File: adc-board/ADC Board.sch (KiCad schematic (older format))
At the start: 62 parts, among them J2 ST-LINK/V2, J3 USART3, J4 USART1, J5 UE27AC5410H, J7 AltPowerInput, J8 USBPowerJumper, J9 USART2, U0 STM32H743ZITx, U10 MCP1501-20E/SN, U13 3.3V Reg, U9 USBLC6-2SC6, Y1 NX3225GD-8.000M-EXS00A-CG04874

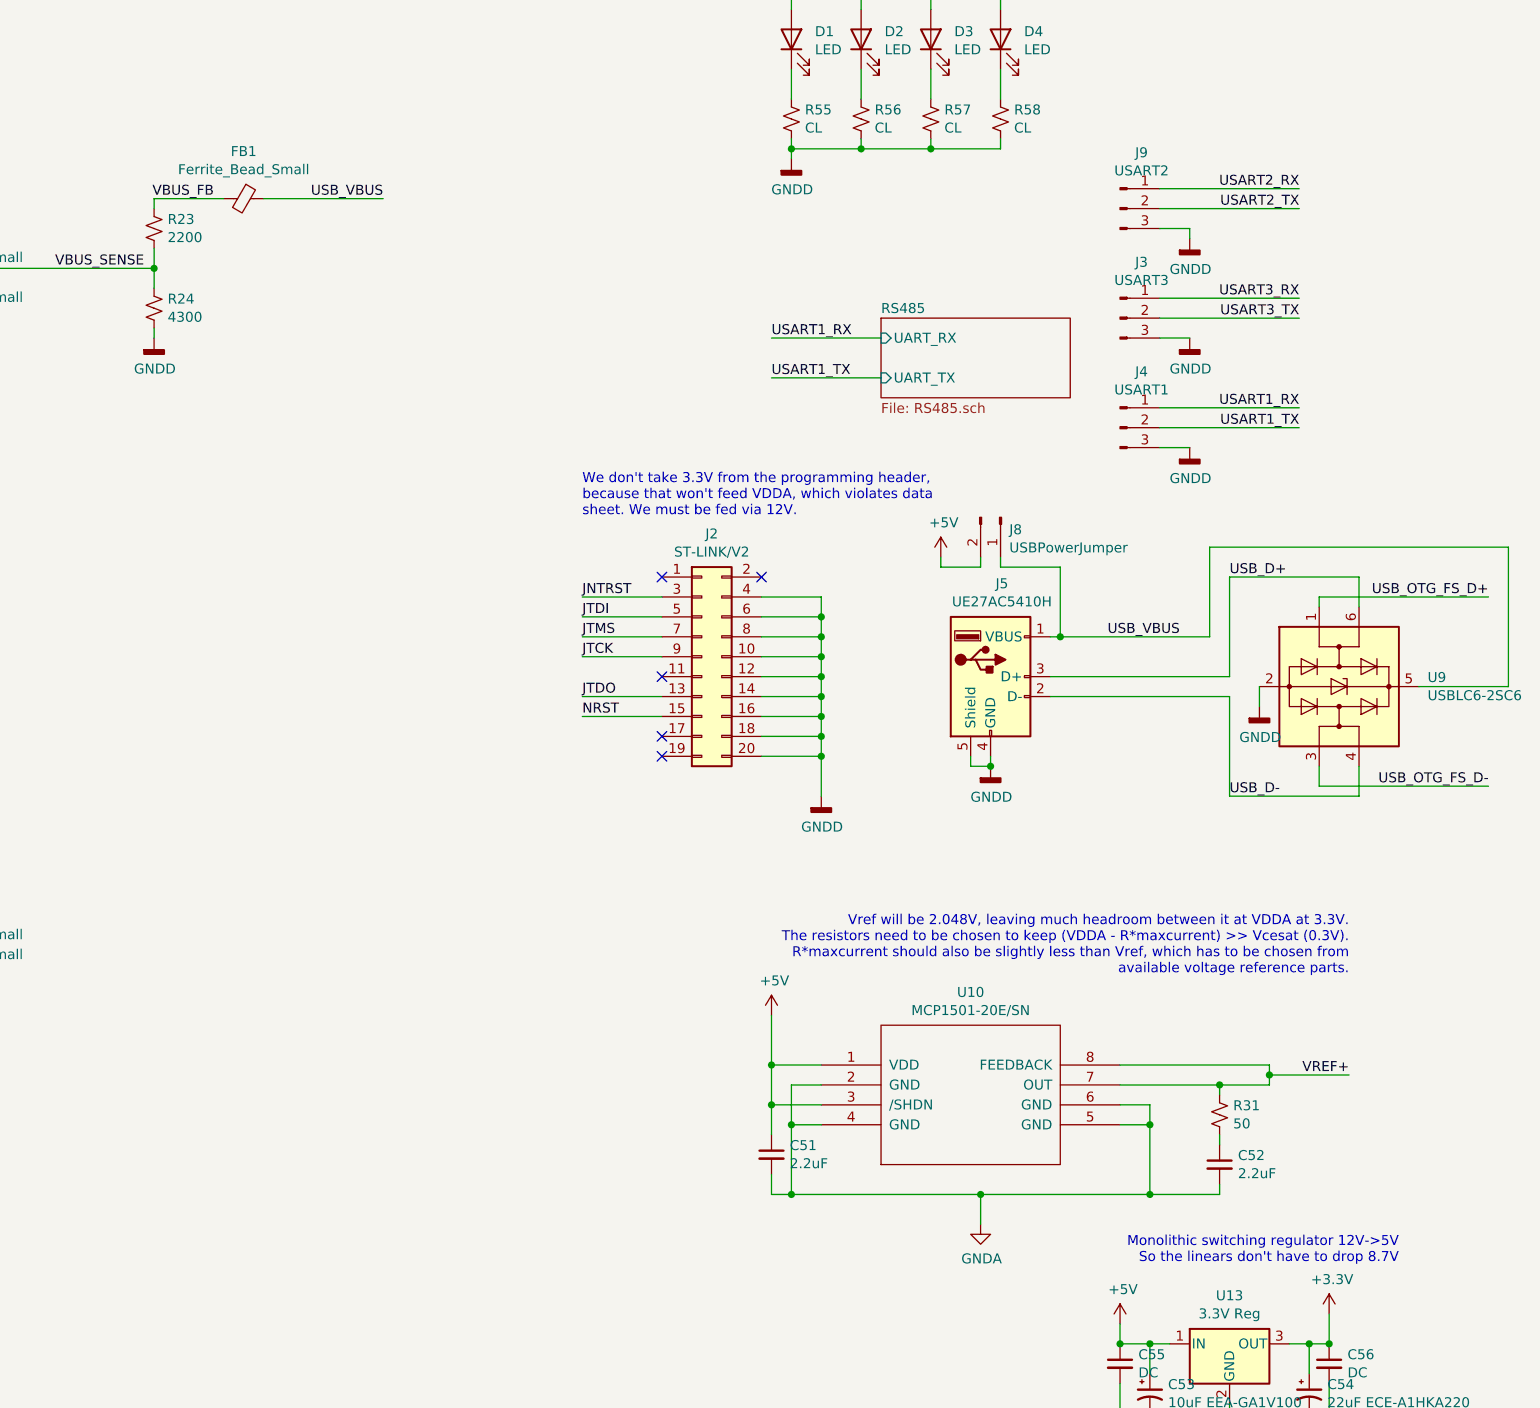
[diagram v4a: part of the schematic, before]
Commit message: move USB ferrite closer to connector; add VCC pad near BOOT pulldown
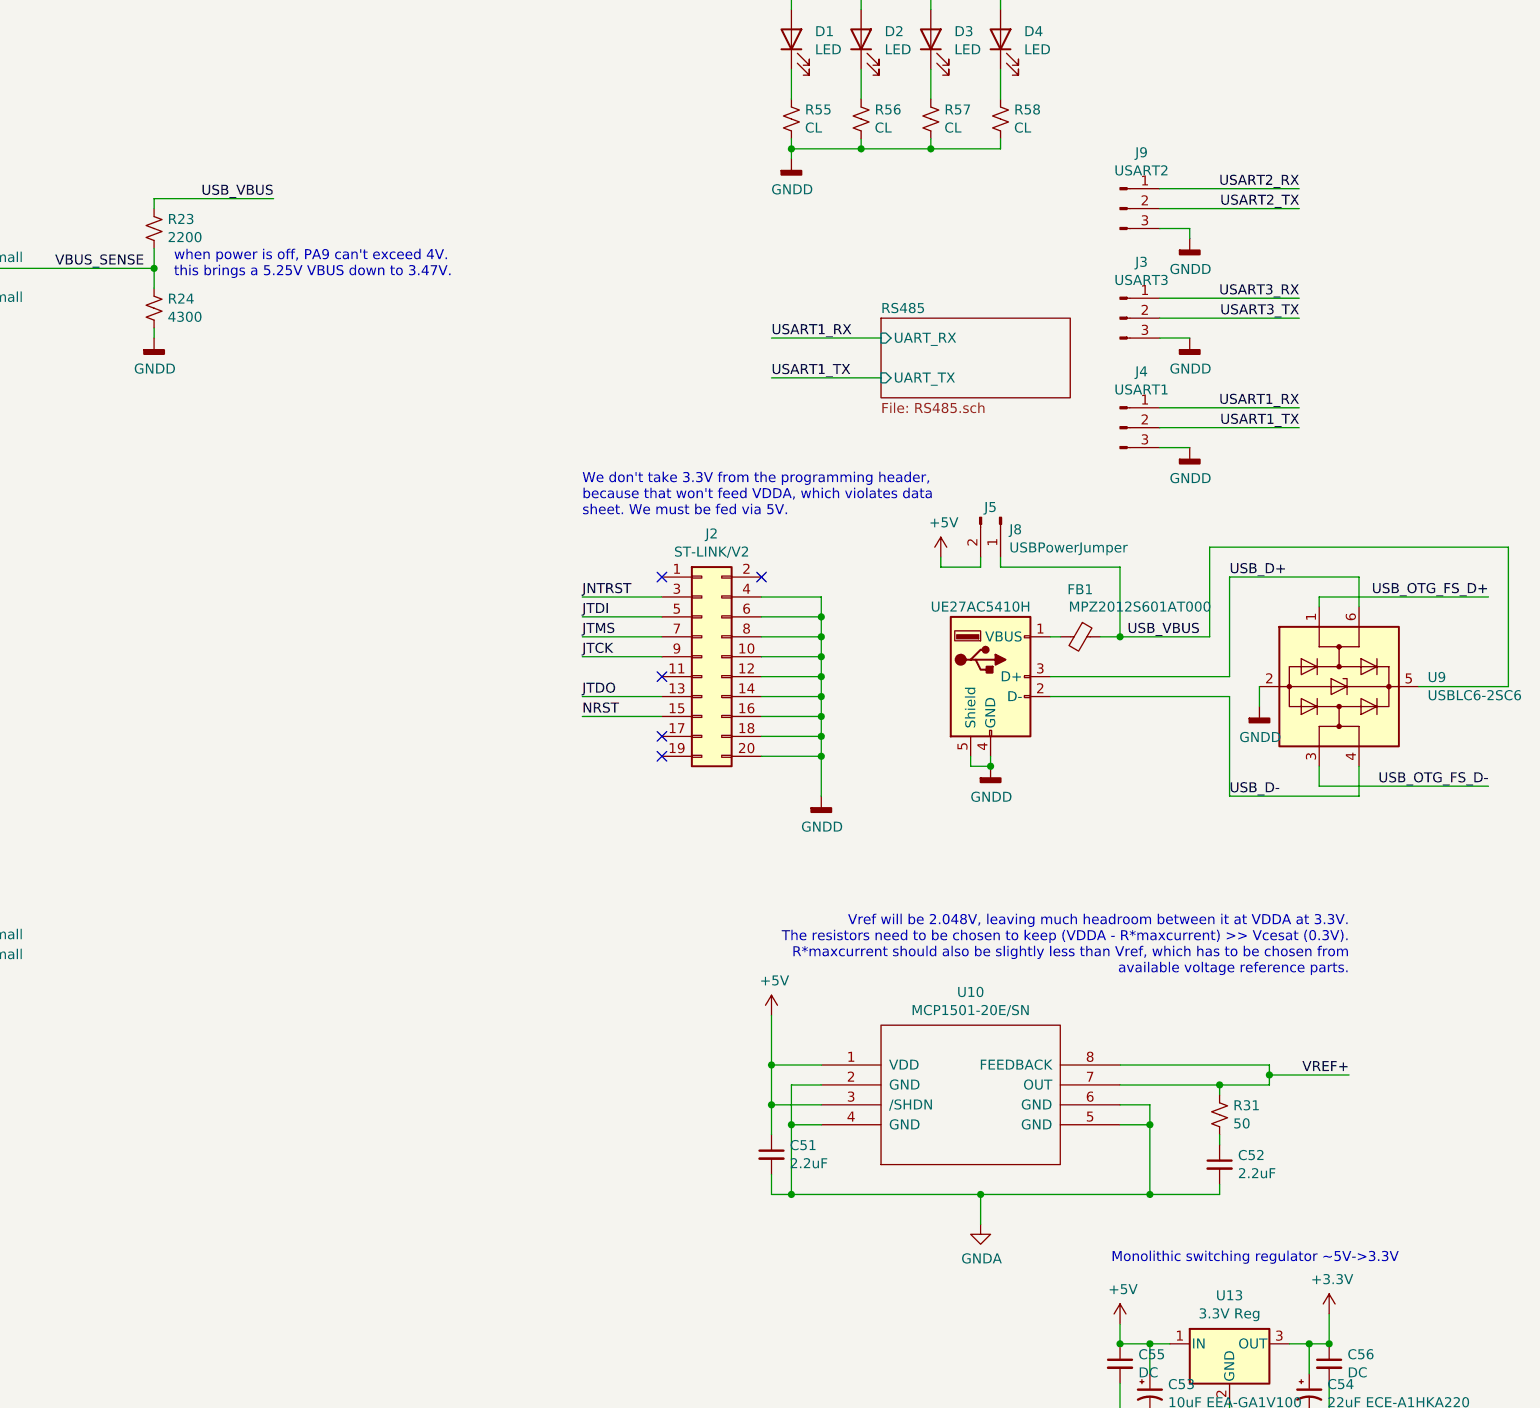
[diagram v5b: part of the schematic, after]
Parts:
- FB1: value Ferrite_Bead_Small -> MPZ2012S601AT000
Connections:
- net USB_VBUS: now also R23.1; no longer J5.1 (VBUS)
- net VBUS_FB: no longer names the net of FB1.2
- net VBUS_FB: now also J5.1 (VBUS); no longer R23.1
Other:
- note added: "Monolithic switching regulator ~~5V->3.3V"
- note added: "We don't take 3.3V from the programming header,\nbecause that won't feed VDDA, which violates data\nsheet. We must be fed via 5V."
- note added: "when power is off, PA9 can't exceed 4V.\nthis brings a 5.25V VBUS down to 3.47V."
- note removed: "Monolithic switching regulator 12V->5V\nSo the linears don't have to drop 8.7V"
- note removed: "We don't take 3.3V from the programming header,\nbecause that won't feed VDDA, which violates data\nsheet. We must be fed via 12V."
- moved on the sheet: FB1
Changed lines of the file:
@@
 U 1 1 62BFF5D3
 P 12500 5300
-F 0 "J5" H 12557 5767 50  0000 C CNN
-F 1 "UE27AC5410H" H 12557 5676 50  0000 C CNN
+F 0 "J5" H 12500 6150 50  0000 C CNN
+F 1 "UE27AC5410H" H 12450 5650 50  0000 C CNN
 F 2 "usbconnectors:USB_A_Molex_67643_Horizontal" H 12650 5250 50  0001 C CNN
 F 3 " ~" H 12650 5250 50  0001 C CNN
@@
 Reference STMicroelectronics Application Note AN4938\nfor details on basic STMH74x circuits
 Text Notes 14550 8250 2    50   ~ 0
-Monolithic switching regulator 12V->5V\nSo the linears don't have to drop 8.7V
+Monolithic switching regulator ~~5V->3.3V
 Text Notes 13850 9700 0    50   ~ 0
 Represents single connection between GNDD and GNDA\nnear the 5V regulator. Could be cut and choke inserted.
@@
 Don't intend to need this crystal circuit
 Text Notes 10450 4500 0    50   ~ 0
-We don't take 3.3V from the programming header,\nbecause that won't feed VDDA, which violates data\nsheet. We must be fed via 12V.
+We don't take 3.3V from the programming header,\nbecause that won't feed VDDA, which violates data\nsheet. We must be fed via 5V.
 Wire Wire Line
 	1300 1550 1000 1550
@@
 $EndComp
 Wire Wire Line
-	12800 5100 12850 5100
-Wire Wire Line
-	12850 5100 12850 4750
-Wire Wire Line
-	12850 4750 12550 4750
+	13150 5100 13150 4750
+Wire Wire Line
+	13150 4750 12550 4750
 Wire Wire Line
 	12550 4750 12550 4700
@@
 Wire Wire Line
 	12800 5400 13700 5400
-Connection ~ 12850 5100
-Text Label 13450 5100 2    50   ~ 0
+Connection ~ 13150 5100
+Text Label 13550 5100 2    50   ~ 0
 USB_VBUS
 Wire Wire Line
@@
 Wire Wire Line
 	8300 2950 8300 2900
-Wire Wire Line
-	8300 2900 8650 2900
 $Comp
 L power:GNDD #PWR0145
@@
 L Device:Ferrite_Bead_Small FB1
 U 1 1 5FC76527
-P 8750 2900
-F 0 "FB1" V 8513 2900 50  0000 C CNN
-F 1 "Ferrite_Bead_Small" V 8604 2900 50  0000 C CNN
-F 2 "Inductors_SMD:L_0805" V 8680 2900 50  0001 C CNN
-F 3 "~" H 8750 2900 50  0001 C CNN
-	1    8750 2900
+P 12950 5100
+F 0 "FB1" V 12713 5100 50  0000 C CNN
+F 1 "MPZ2012S601AT000" V 12800 5400 50  0000 C CNN
+F 2 "Inductors_SMD:L_0805" V 12880 5100 50  0001 C CNN
+F 3 "~" H 12950 5100 50  0001 C CNN
+	1    12950 5100
 	0    1    1    0
 $EndComp
 Wire Wire Line
-	8850 2900 9450 2900
-Text Label 9450 2900 2    50   ~ 0
+	8300 2900 8900 2900
+Text Label 8900 2900 2    50   ~ 0
 USB_VBUS
 Text Label 8250 3250 2    50   ~ 0
 VBUS_SENSE
-Text Label 8600 2900 2    50   ~ 0
-VBUS_FB
 NoConn ~ 6350 6450
 NoConn ~ 3850 5450
@@
 	15100 5350 14650 5350
 Wire Wire Line
-	12850 5100 13600 5100
+	13150 5100 13600 5100
+Text Notes 8400 3300 0    50   ~ 0
+when power is off, PA9 can't exceed 4V.\nthis brings a 5.25V VBUS down to 3.47V.
+Wire Wire Line
+	12800 5100 12850 5100
+Wire Wire Line
+	13050 5100 13150 5100
 $EndSCHEMATC

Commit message: Rev0 of boards; added text
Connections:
- net +3.3VA: now also C51.1, U10.1 (VDD), U10.3 (/SHDN)
- net +5V: no longer C51.1, U10.1 (VDD), U10.3 (/SHDN)
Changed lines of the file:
@@
 Wire Wire Line
 	11400 7250 11400 7000
-$Comp
-L power:+5V #PWR0126
-U 1 1 61B1F663
-P 11400 7000
-F 0 "#PWR0126" H 11400 6850 50  0001 C CNN
-F 1 "+5V" H 11415 7173 50  0000 C CNN
-F 2 "" H 11400 7000 50  0001 C CNN
-F 3 "" H 11400 7000 50  0001 C CNN
-	1    11400 7000
-	1    0    0    -1
-$EndComp
 Wire Wire Line
 	11650 7350 11500 7350
@@
 Wire Wire Line
 	13050 5100 13150 5100
+$Comp
+L power:+3.3VA #PWR?
+U 1 1 5FBE27C1
+P 11400 7000
+F 0 "#PWR?" H 11400 6850 50  0001 C CNN
+F 1 "+3.3VA" H 11415 7173 50  0000 C CNN
+F 2 "" H 11400 7000 50  0001 C CNN
+F 3 "" H 11400 7000 50  0001 C CNN
+	1    11400 7000
+	1    0    0    -1
+$EndComp
 $EndSCHEMATC

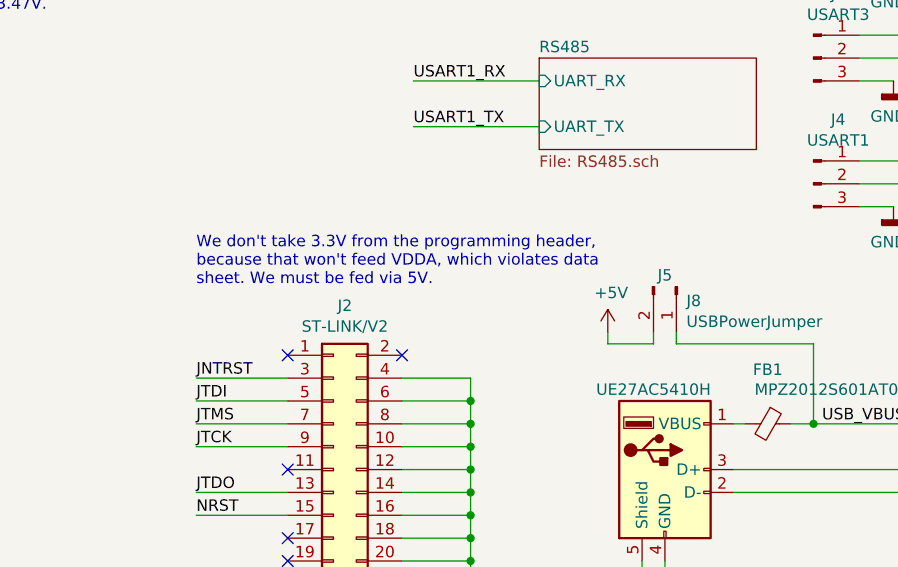
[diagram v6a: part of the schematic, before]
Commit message: correct the jtag header
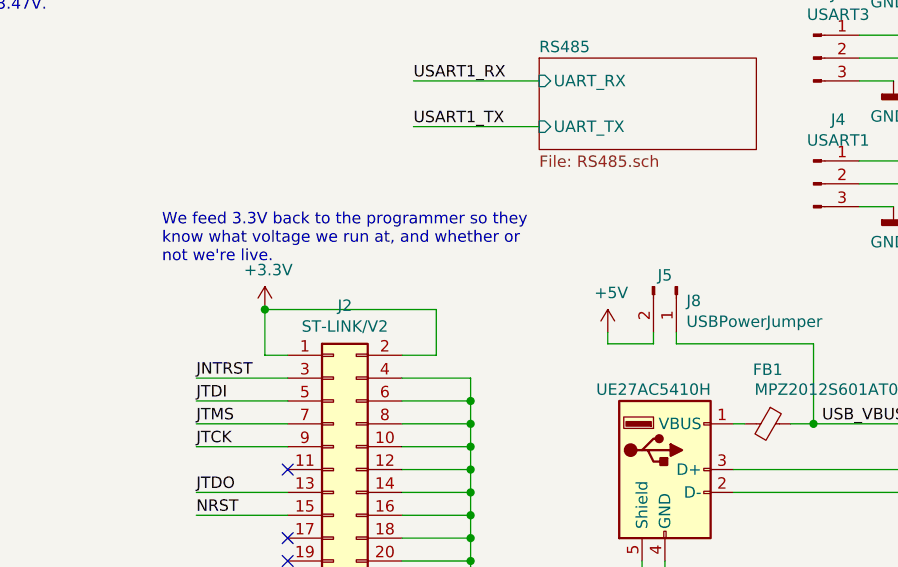
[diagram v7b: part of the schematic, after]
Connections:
- net +3V3: now also J2.1 (Pin_1), J2.2 (Pin_2)
- no-connect marks 71 -> 69
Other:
- note added: "We feed 3.3V back to the programmer so they\nknow what voltage we run at, and whether or\nnot we're live."
- note removed: "We don't take 3.3V from the programming header,\nbecause that won't feed VDDA, which violates data\nsheet. We must be fed via 5V."
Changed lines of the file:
@@
 Wire Wire Line
 	13700 8950 13700 9050
-NoConn ~ 10850 4800
-NoConn ~ 11350 4800
 $Comp
 L Device:CP1_Small C53
@@
 Text Notes 2150 4050 0    50   ~ 0
 Don't intend to need this crystal circuit
-Text Notes 10450 4500 0    50   ~ 0
-We don't take 3.3V from the programming header,\nbecause that won't feed VDDA, which violates data\nsheet. We must be fed via 5V.
+Text Notes 10300 4400 0    50   ~ 0
+We feed 3.3V back to the programmer so they\nknow what voltage we run at, and whether or\nnot we're live.
 Wire Wire Line
 	1300 1550 1000 1550
@@
 	1    0    0    -1
 $EndComp
+$Comp
+L power:+3.3V #PWR?
+U 1 1 5FBC7EC8
+P 10750 4600
+F 0 "#PWR?" H 10750 4450 50  0001 C CNN
+F 1 "+3.3V" H 10765 4773 50  0000 C CNN
+F 2 "" H 10750 4600 50  0001 C CNN
+F 3 "" H 10750 4600 50  0001 C CNN
+	1    10750 4600
+	1    0    0    -1
+$EndComp
+Wire Wire Line
+	10750 4800 10850 4800
+Wire Wire Line
+	10750 4600 11500 4600
+Wire Wire Line
+	11500 4600 11500 4800
+Wire Wire Line
+	11500 4800 11350 4800
+Connection ~ 10750 4600
+Wire Wire Line
+	10750 4600 10750 4800
 $EndSCHEMATC
